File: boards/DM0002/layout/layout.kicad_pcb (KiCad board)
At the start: 4 copper layers, 15 x 38.6 mm, 57 parts, among them J1 62201021121, J2 USB4105-GF-A, SW1 KMR231G LFS, U1 TLV75801PDRVR, U2 W25Q16JVUXIQ, U3 RP2040, U4 SG-210STF 12.0000ML0

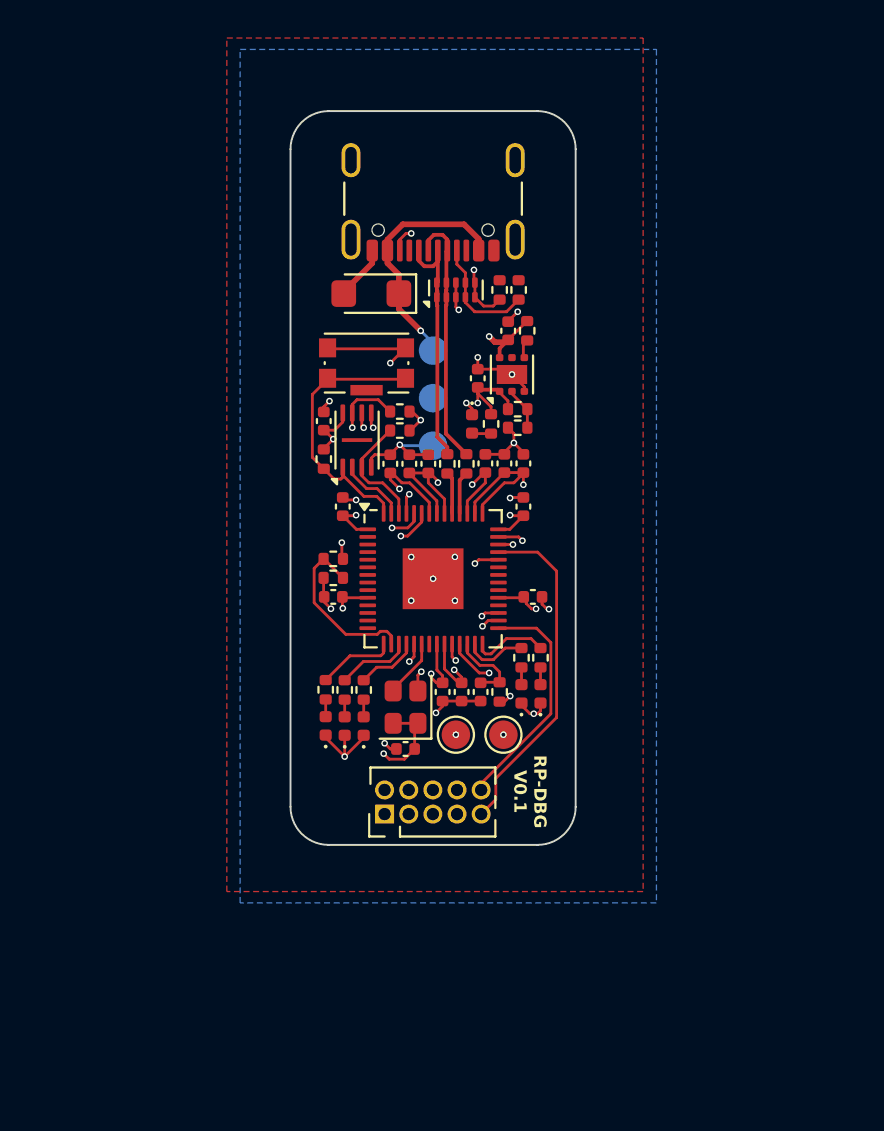
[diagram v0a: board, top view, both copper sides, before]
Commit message: fully routed
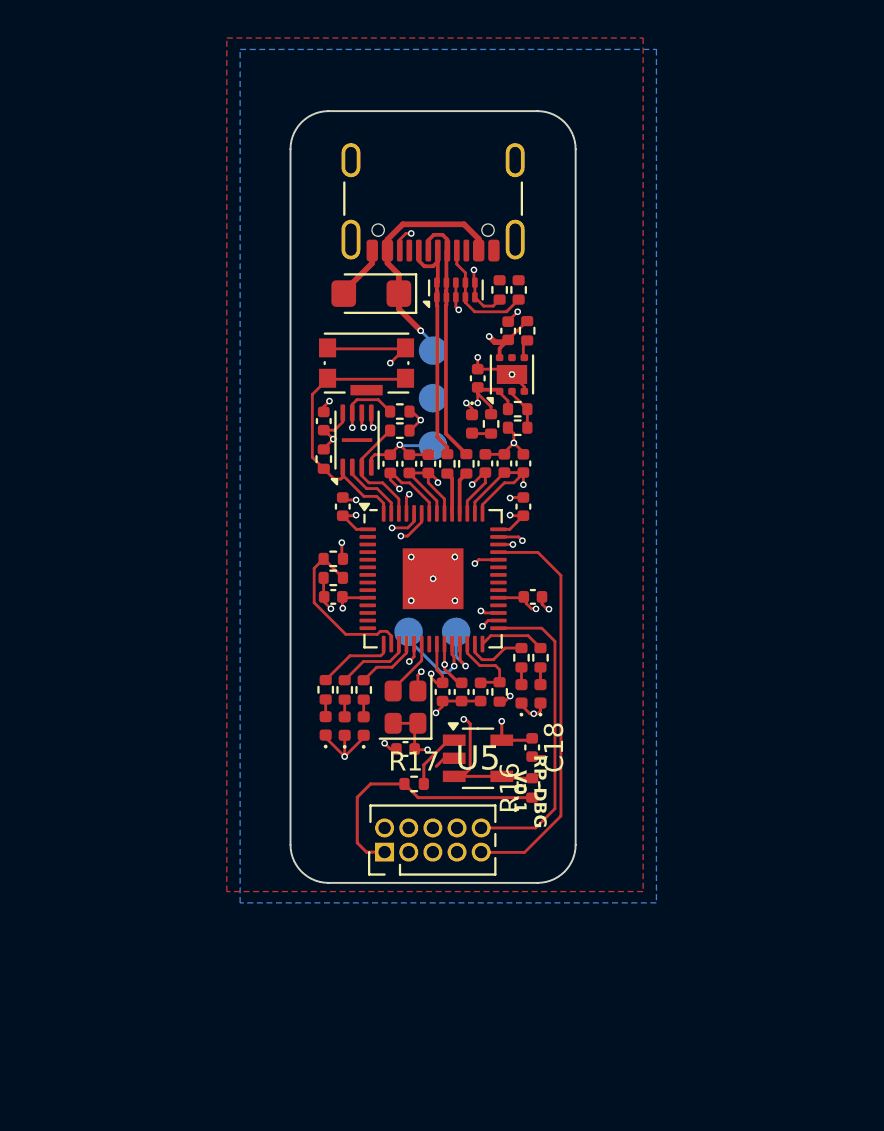
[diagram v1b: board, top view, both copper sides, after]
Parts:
- added C18: GCM155R71H104KE02D, C_0402_1005Metric:C_0402_1005Metric, F.Cu at (45.6, 76.9)
- added R16: ERJ-2GE0R00X, R_0402_1005Metric:R_0402_1005Metric, F.Cu at (45.6, 79.0)
- added R17: ERJ-2RKF1002X, R_0402_1005Metric:R_0402_1005Metric, F.Cu at (39.4, 78.8)
- added U5: TLV9001IDBVR, SOT95P280X145-5N:SOT95P280X145-5N, F.Cu at (42.8, 77.5)
- TP2, TP3: moved to B.Cu
- moved TP2 5.95 mm to (39.1, 70.8), turned to 180 degrees
- moved TP3 5.95 mm to (41.6, 70.8), turned to 180 degrees
- moved J1 2.00 mm to (37.8, 82.4)
- renumbered R16 to R18, R17 to R19, R18 to R20, R19 to R21
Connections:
- U3 pad 38: TARGET_V_SENSE -> TARGET_V_SENSE_BUFFER
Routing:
- net TARGET_V_SENSE_BUFFER: track 0.00 -> 18.2 mm, vias 0 -> 2
- net TARGET_V_SENSE: track 18.9 -> 13.8 mm, vias 1 -> 0
- net TARGET_RESET: track 12.3 -> 16.4 mm
- net TARGET_GND_DETECT: track 17.9 -> 21.4 mm
- net TARGET_V_SENSE_R: track 0.00 -> 3.14 mm
- net MCU.SWD_SWDIO: track 6.03 -> 3.29 mm, vias 2 -> 1
- net SWD_SWDIO: track 13.4 -> 15.4 mm
- net GND: track 40.5 -> 42.3 mm
- net SWD_SWCLK: track 11.9 -> 13.6 mm
- net TARGET_UART_TX: track 16.7 -> 18.0 mm
- net VDD_3V3: track 41.7 -> 43.0 mm, vias 12 -> 13
- net TARGET_UART_RX: track 16.9 -> 17.8 mm
- net LED_B: track 4.02 -> 3.50 mm
- net MCU.SWD_SWCLK: track 5.16 -> 4.87 mm, vias 2 -> 1
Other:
- board size 15 x 38.6 mm -> 15 x 40.6 mm

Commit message: IO reassignments routed
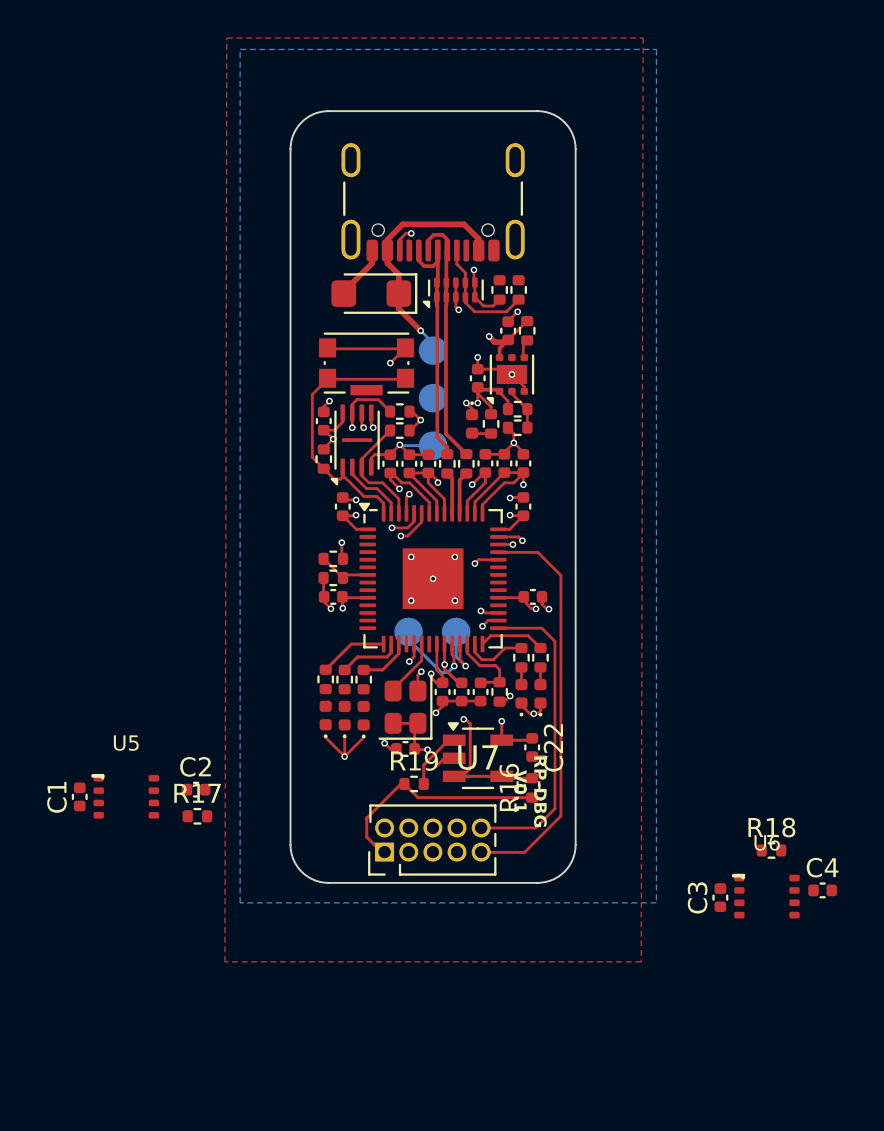
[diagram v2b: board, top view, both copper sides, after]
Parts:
- added C1: GCM155R71H104KE02D, C_0402_1005Metric:C_0402_1005Metric, F.Cu at (21.8, 79.5)
- added C2: GCM155R71H104KE02D, C_0402_1005Metric:C_0402_1005Metric, F.Cu at (27.9, 79.1)
- added C3: GCM155R71H104KE02D, C_0402_1005Metric:C_0402_1005Metric, F.Cu at (55.5, 84.8)
- added C4: GCM155R71H104KE02D, C_0402_1005Metric:C_0402_1005Metric, F.Cu at (60.9, 84.4)
- added R17: ERJ-2RKF1002X, R_0402_1005Metric:R_0402_1005Metric, F.Cu at (28.0, 80.5)
- added R18: ERJ-2RKF1002X, R_0402_1005Metric:R_0402_1005Metric, F.Cu at (58.2, 82.3)
- added U5: TXB0102DCUR, SOP65P250X110-8N:SOP65P250X110-8N, F.Cu at (24.2, 79.5)
- added U6: TXB0102DCUR, SOP65P250X110-8N:SOP65P250X110-8N, F.Cu at (58.0, 84.7)
- moved D3 0.55 mm to (36.7, 75.2)
- moved D4 0.55 mm to (35.7, 75.2)
- moved D5 0.55 mm to (34.7, 75.2)
- moved R6 0.55 mm to (36.7, 73.3)
- moved R7 0.55 mm to (35.7, 73.3)
- moved R8 0.55 mm to (34.7, 73.3)
- renumbered C6 to C10, C7 to C11, C8 to C12, C9 to C13, C10 to C14, C11 to C15, C12 to C16, C13 to C17, C14 to C18, C15 to C19, C16 to C20, C17 to C21, C18 to C22, C1 to C5, C2 to C6, C3 to C7, C4 to C8, C5 to C9, R17 to R19, R18 to R20, R19 to R21, R20 to R22, R21 to R23, U5 to U7
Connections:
- net TARGET_V_SENSE renamed TARGET_VDDIO
- U3 pad 16: VBUS_DET -> LED_O2
- U3 pad 17: LED_O2 -> LED_O1
- U3 pad 18: LED_O1 -> MCU.GPIO15
- U3 pad 30: SWD_SWCLK -> MCU_SWCLK
- U3 pad 31: SWD_SWDIO -> MCU_SWDIO
- U3 pad 32: MCU.GPIO21 -> SWD_LS_OE
- U3 pad 34: MCU.GPIO22 -> UART_LS_OE
- U3 pad 40: TARGET_UART_RX -> MCU_UART_RX
- U3 pad 41: TARGET_UART_TX -> MCU_UART_TX
- U3 pad 7: MCU.GPIO5 -> VBUS_DET
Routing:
- net VBUS_DET: track 9.29 -> 2.80 mm
- net TARGET_VDDIO: track 13.8 -> 12.0 mm
- net LED_O3.LED_R_NET: track 0.91 -> 0.00 mm
- net LED_O2.LED_R_NET: track 0.91 -> 0.00 mm
- net LED_O1.LED_R_NET: track 0.91 -> 0.00 mm
- net LED_O2: track 3.90 -> 3.28 mm
- net LED_O1: track 3.31 -> 2.71 mm

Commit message: board outline expanded a couple mm, level shifters added. committing before further adjusting GPIO assignments
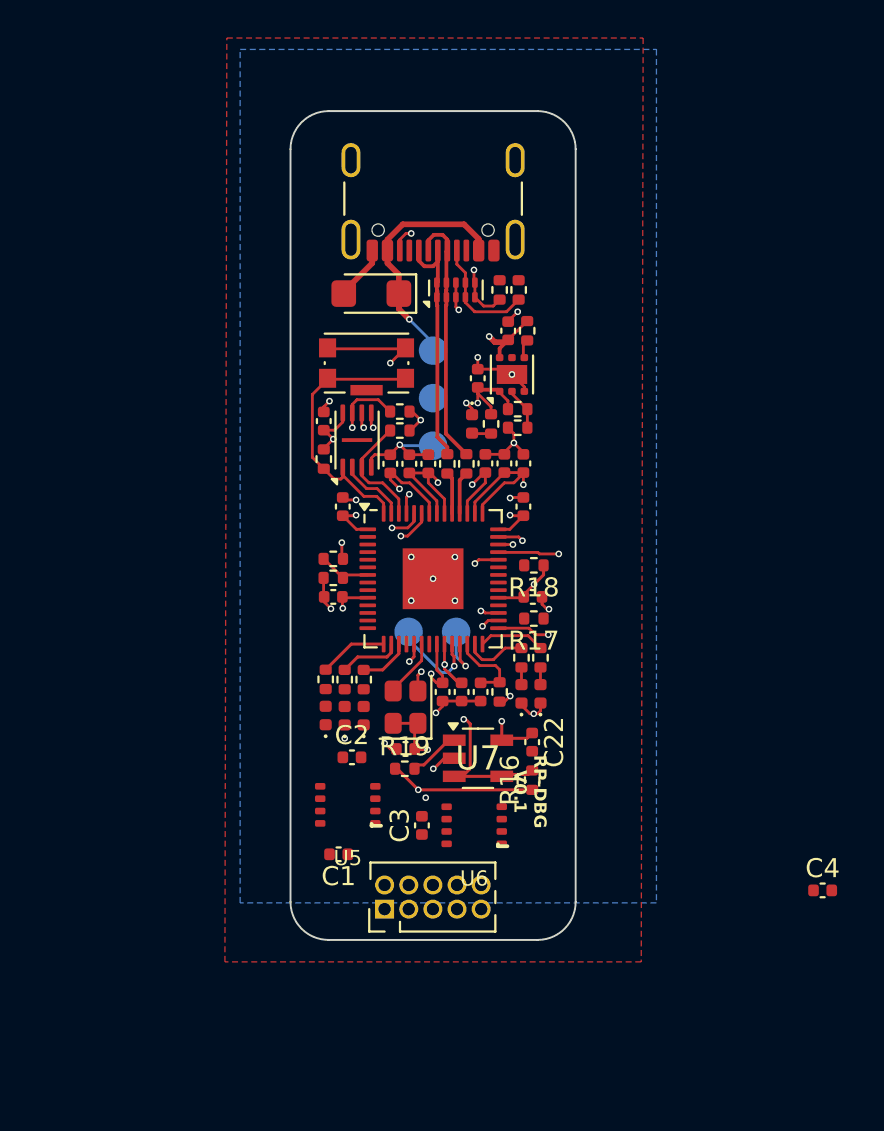
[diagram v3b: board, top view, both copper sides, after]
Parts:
- moved R17 20.5 mm to (45.7, 70.1), turned to 180 degrees
- moved R18 19.5 mm to (45.7, 67.3), turned to 180 degrees
- moved C3 16.2 mm to (39.8, 81.0)
- moved U6 15.9 mm to (42.5, 81.0), turned to 180 degrees
- moved C1 14.0 mm to (35.4, 82.5), turned to 180 degrees
- moved U5 11.7 mm to (35.9, 79.9), turned to 180 degrees
- moved C2 8.37 mm to (36.1, 77.4)
- moved J1 3.00 mm to (37.8, 85.4)
- moved R19 0.94 mm to (38.9, 78.0)
- moved R16 0.41 mm to (45.6, 78.6)
- moved C22 0.28 mm to (45.6, 76.6)
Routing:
- net TARGET_UART_TX: track 18.0 -> 0.00 mm, vias 1 -> 0
- net MCU_UART_TX: track 0.00 -> 18.0 mm, vias 0 -> 1
- net TARGET_UART_RX: track 17.8 -> 0.00 mm, vias 1 -> 0
- net MCU_UART_RX: track 0.00 -> 17.8 mm, vias 0 -> 1
- net SWD_SWDIO: track 15.4 -> 0.00 mm, vias 1 -> 0
- net SWD_SWCLK: track 13.6 -> 0.00 mm, vias 1 -> 0
- net MCU_SWCLK: track 0.00 -> 13.6 mm, vias 0 -> 1
- net MCU_SWDIO: track 0.00 -> 12.5 mm, vias 0 -> 2
- net GND: track 42.1 -> 37.4 mm, vias 24 -> 25
- net TARGET_VDDIO: track 12.0 -> 7.67 mm, vias 0 -> 1
- net TARGET_GND_DETECT: track 21.4 -> 24.6 mm, vias 0 -> 1
- net TARGET_RESET: track 16.4 -> 18.5 mm, vias 0 -> 1
- net VDD_3V3: track 43.0 -> 44.2 mm
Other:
- board size 15 x 40.6 mm -> 15 x 43.6 mm

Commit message: more IO assignment adjustment & more layout progress
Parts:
- moved C4 20.6 mm to (40.5, 81.6), turned to 180 degrees
- moved R18 11.3 mm to (35.1, 71.2), turned to 0 degrees
- moved R17 10.6 mm to (35.1, 70.2), turned to 0 degrees
- moved C3 6.60 mm to (46.4, 81.2), turned to -90 degrees
- moved C1 5.50 mm to (40.5, 80.4), turned to 0 degrees
- moved C2 4.20 mm to (34.5, 81.3), turned to -90 degrees
- moved U5 1.55 mm to (37.1, 80.9)
- moved U6 1.25 mm to (43.8, 80.9)
- moved R19 0.71 mm to (39.4, 78.5), turned to 90 degrees
- moved C10 0.54 mm to (45.6, 69.5)
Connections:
- U3 pad 13: MCU.GPIO10 -> SWD_LS_OE
- U3 pad 14: MCU.GPIO11 -> UART_LS_OE
- U3 pad 32: SWD_LS_OE -> MCU.GPIO21
- U3 pad 34: UART_LS_OE -> MCU.GPIO22
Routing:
- net SWD_LS_OE: track 0.00 -> 15.1 mm, vias 0 -> 2
- net MCU_SWDIO: track 12.5 -> 16.9 mm
- net MCU_UART_RX: track 17.8 -> 14.4 mm
- net UART_LS_OE: track 0.00 -> 2.79 mm, vias 0 -> 1
- net MCU_UART_TX: track 18.0 -> 15.5 mm
- net TARGET_VDDIO: track 7.67 -> 6.24 mm, vias 1 -> 0
- net GND: track 37.4 -> 36.4 mm, vias 25 -> 24
- net VDD_3V3: track 44.2 -> 45.2 mm
- net TARGET_GND_DETECT: track 24.6 -> 25.3 mm
- net TARGET_RESET: track 18.5 -> 19.0 mm
- net MCU_SWCLK: track 13.6 -> 13.7 mm, vias 1 -> 2

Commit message: all nets routed
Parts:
- moved C3 0.52 mm to (46.4, 81.7)
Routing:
- net TARGET_VDDIO: track 6.24 -> 31.1 mm, vias 0 -> 2
- net UART_LS_OE: track 2.79 -> 21.5 mm, vias 1 -> 2
- net TARGET_UART_TX: track 0.00 -> 4.54 mm
- net VDD_3V3: track 45.2 -> 48.9 mm, vias 13 -> 15
- net TARGET_UART_RX: track 0.00 -> 3.26 mm
- net SWD_SWDIO: track 0.00 -> 3.17 mm
- net MCU_UART_RX: track 14.4 -> 17.5 mm, vias 1 -> 2
- net SWD_SWCLK: track 0.00 -> 2.50 mm
- net TARGET_GND_DETECT: track 25.3 -> 24.1 mm
- net LED_O3.LED_R_NET: track 0.00 -> 0.91 mm
- net LED_O2.LED_R_NET: track 0.00 -> 0.91 mm
- net LED_O1.LED_R_NET: track 0.00 -> 0.91 mm
- net MCU_UART_TX: track 15.5 -> 16.2 mm, vias 1 -> 2
- net GND: track 36.4 -> 36.6 mm, vias 24 -> 30

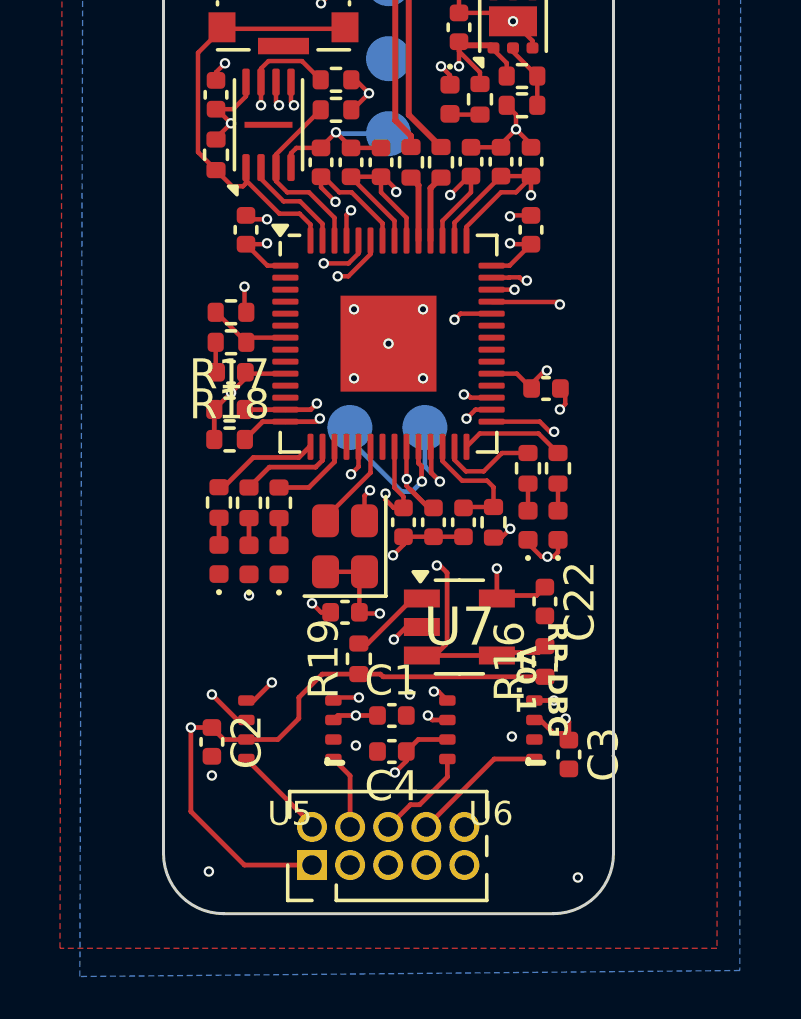
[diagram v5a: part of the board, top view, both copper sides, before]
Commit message: logo and version number added to layout
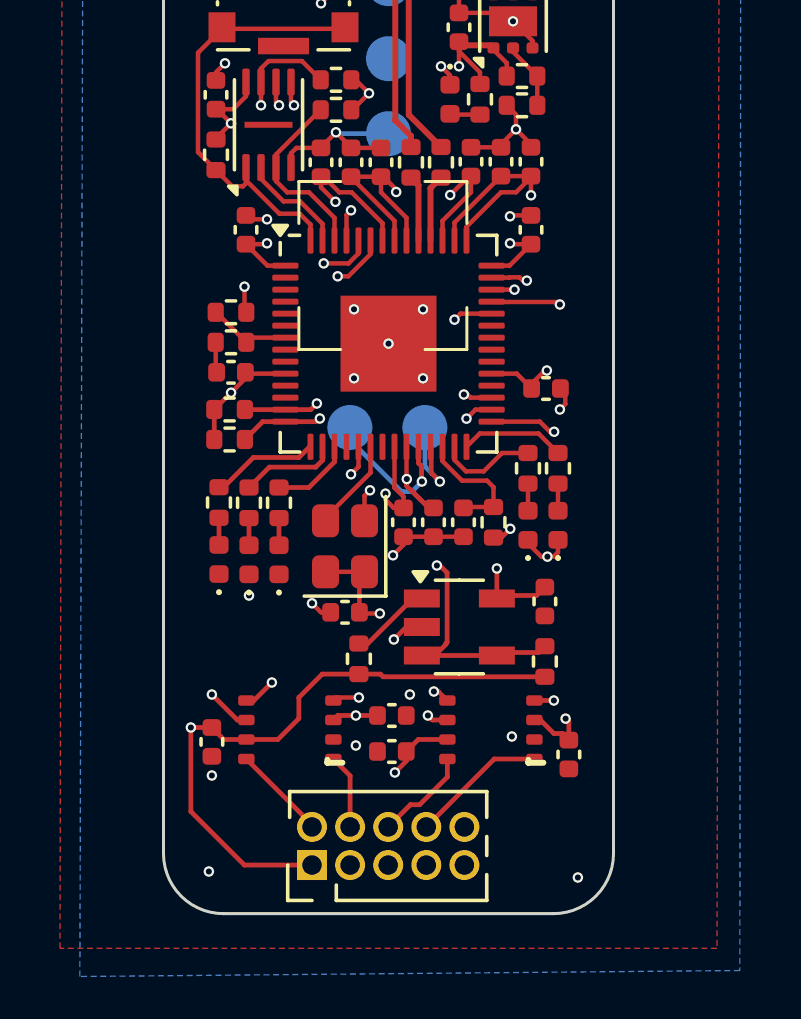
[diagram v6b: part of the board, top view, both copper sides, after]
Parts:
- added V1: ?, version-footprint:version-footprint, B.Cu at (40.7, 68.8)
- moved TP1 11.6 mm to (45.7, 84.4)
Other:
- board text removed: "RP-DBG V0.1"
